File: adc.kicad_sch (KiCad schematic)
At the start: 24 parts, among them U4 PCM1863DBT

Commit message: Page settings
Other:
- company: (none) -> github.com/pedalboard
- title: (none) -> Open Pedalboard Soundcard
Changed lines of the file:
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@@
 (kicad_sch (version 20230121) (generator eeschema)
   (paper "A4")
+  (title_block
+    (title "Open Pedalboard Soundcard")
+    (date "2023-12-19")
+    (rev "0.0.1")
+    (company "github.com/pedalboard")
+    (comment 1 "Source Code: https://github.com/pedalboard/pedalboard-hw")
+    (comment 2 "License: CERN Open Hardware Licence Version 2 - Permissive")
+  )
   (junction (at 90.17 144.78) (diameter 0) (color 0 0 0 0)
   )

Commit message: Distribute parts on PCB
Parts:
- added J2: Conn_02x03_Odd_Even, Connector_PinHeader_2.54mm:PinHeader_2x03_P2.54mm_Vertical, symbol Connector_Generic:Conn_02x03_Odd_Even
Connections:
- net GND: now also J2.3 (Pin_3), J2.4 (Pin_4)
- net inl+: now also J2.5 (Pin_5)
- net inl-: now also J2.6 (Pin_6)
- net inr+: now also J2.2 (Pin_2)
- net inr-: now also J2.1 (Pin_1)
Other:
- moved on the sheet: R4

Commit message: Cleanup routing
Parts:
- U4: footprint pedalboard-soundcard:PCM1863DBT -> Package_SO:TSSOP-30_4.4x7.8mm_P0.5mm
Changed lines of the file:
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@@
       (effects (font (size 1.524 1.524)))
     )
-    (property "Footprint" "pedalboard-soundcard:PCM1863DBT" (at 113.03 91.186 0)
+    (property "Footprint" "Package_SO:TSSOP-30_4.4x7.8mm_P0.5mm" (at 113.03 91.186 0)
       (effects (font (size 1.524 1.524)) hide)
     )

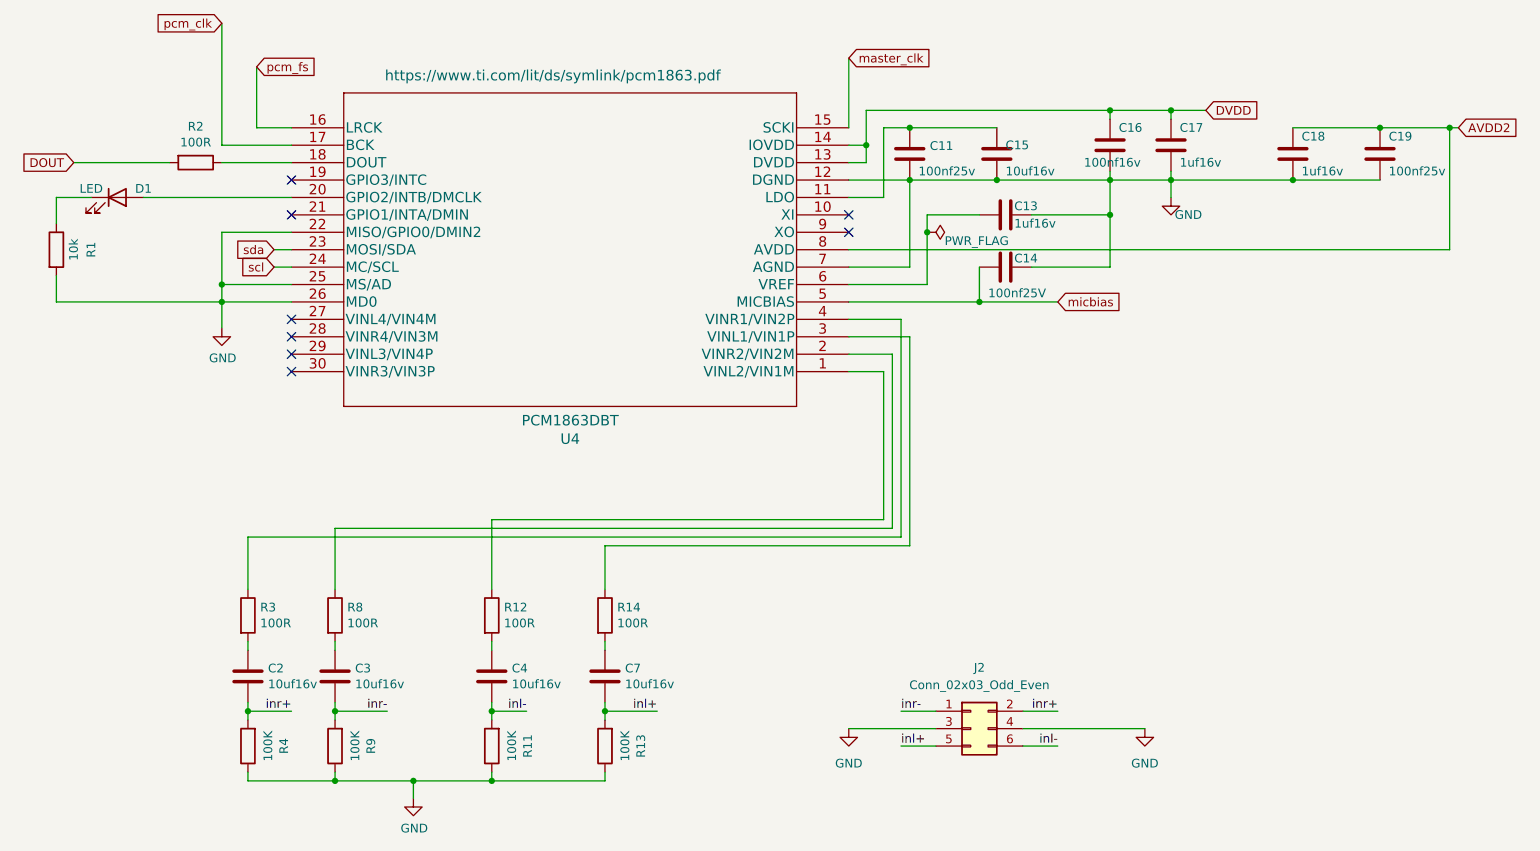
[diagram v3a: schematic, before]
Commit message: improve BOM
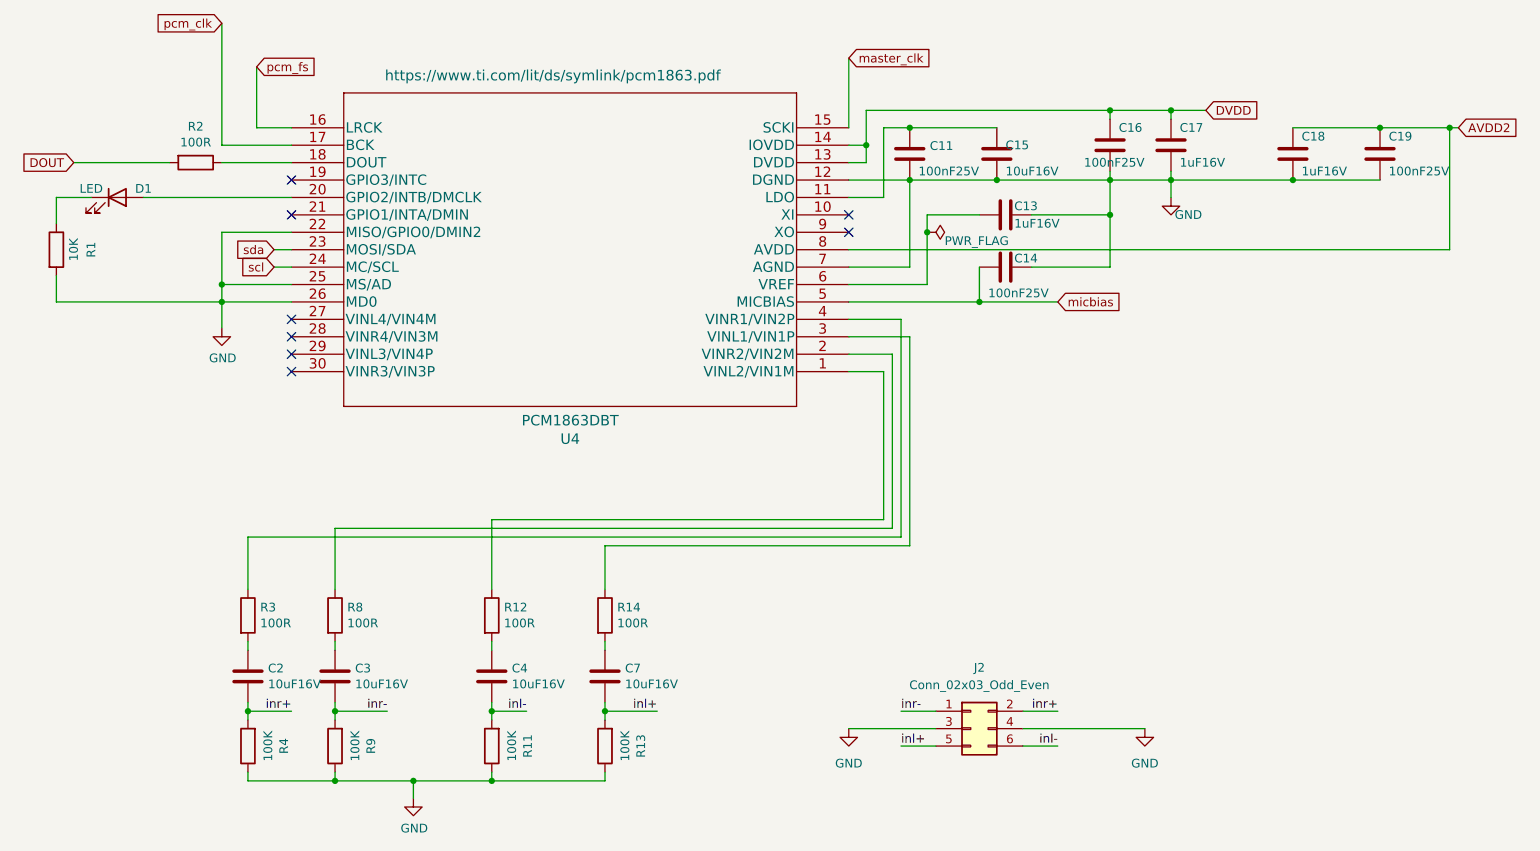
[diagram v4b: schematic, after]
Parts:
- C11, C19: value 100nf25v -> 100nF25V; Supplier (none) -> https://www.digikey.ch/de/products/detail/samsung-electro-m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
- C13, C17, C18: value 1uf16v -> 1uF16V; Supplier (none) -> https://www.digikey.ch/de/products/detail/samsung-electro-m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
- C14: value 100nf25V -> 100nF25V; Supplier (none) -> https://www.digikey.ch/de/products/detail/samsung-electro-m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
- C15, C2, C3, C4, C7: value 10uf16v -> 10uF16V; Supplier (none) -> https://www.digikey.ch/de/products/detail/samsung-electro-m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
- C16: value 100nf16v -> 100nF25V; Supplier (none) -> https://www.digikey.ch/de/products/detail/samsung-electro-m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
- R1: value 10k -> 10K; Supplier (none) -> https://www.digikey.ch/de/products/detail/stackpole-electro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
- R11, R12, R13, R14, R2, R3, R4, R8, R9: Supplier (none) -> https://www.digikey.ch/de/products/detail/stackpole-electro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
- U4: Supplier (none) -> https://www.digikey.ch/de/products/detail/texas-instruments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

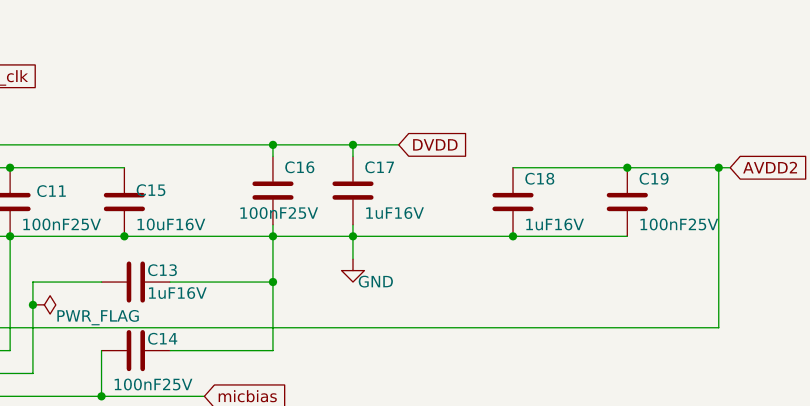
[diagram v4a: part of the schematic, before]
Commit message: Replace DVDD global label with VDD power symbol
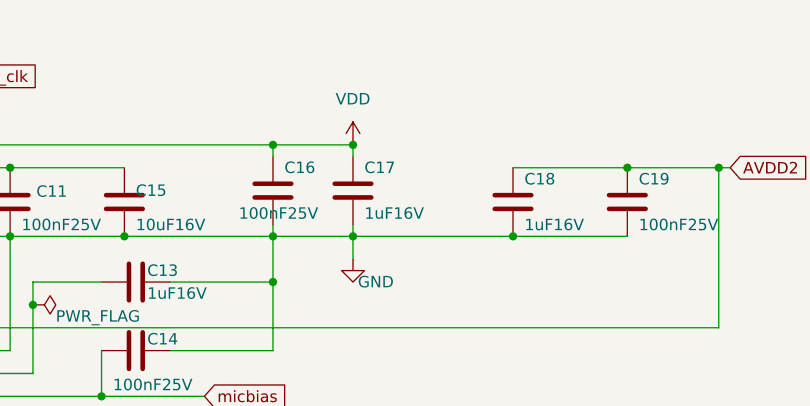
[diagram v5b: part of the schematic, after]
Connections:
- net DVDD renamed VDD
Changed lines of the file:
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@@
   (junction (at 62.23 74.93) (diameter 0) (color 0 0 0 0)
   )
+  (junction (at 200.66 46.99) (diameter 0) (color 0 0 0 0)
+  )
   (junction (at 101.6 144.78) (diameter 0) (color 0 0 0 0)
   )
@@
   )
   (junction (at 172.72 74.93) (diameter 0) (color 0 0 0 0)
-  )
-  (junction (at 200.66 46.99) (diameter 0) (color 0 0 0 0)
   )
   (junction (at 218.44 57.15) (diameter 0) (color 0 0 0 0)
@@
     (stroke (width 0) (type default))
   )
-  (wire (pts (xy 205.74 46.99) (xy 200.66 46.99))
-    (stroke (width 0) (type default))
-  )
   (wire (pts (xy 101.6 134.62) (xy 106.68 134.62))
     (stroke (width 0) (type default))
@@
     )
   )
-  (global_label "DVDD" (shape input) (at 205.74 46.99 0)
-    (effects (font (size 1.27 1.27)) (justify left))
-    (property "Intersheetrefs" "${INTERSHEET_REFS}" (at 205.74 46.99 0)
-      (effects (font (size 1.27 1.27)) hide)
-    )
-  )
   (global_label "AVDD2" (shape input) (at 242.57 49.53 0)
     (effects (font (size 1.27 1.27)) (justify left))
@@
         )
       )
+    )
+  )
+  (symbol (lib_id "power:VDD") (at 200.66 46.99 0) (unit 1)
+    (in_bom yes) (on_board yes) (dnp no) (fields_autoplaced)
+    (property "Reference" "#PWR023" (at 200.66 50.8 0)
+      (effects (font (size 1.27 1.27)) hide)
+    )
+    (property "Value" "VDD" (at 200.66 41.91 0)
+      (effects (font (size 1.27 1.27)))
+    )
+    (property "Footprint" "" (at 200.66 46.99 0)
+      (effects (font (size 1.27 1.27)) hide)
+    )
+    (property "Datasheet" "" (at 200.66 46.99 0)
+      (effects (font (size 1.27 1.27)) hide)
+    )
+    (pin "1")
+    (instances
+      (project "pedalboard-soundcard"
+        (path "/257597c6-fbef-4478-b0f4-968f2d6f1866/7494c0d8-b421-47d6-807b-2365bb2b2e5f"
+          (reference "#PWR023") (unit 1)
+        )
+      )
